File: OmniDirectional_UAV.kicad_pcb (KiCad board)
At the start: 2 copper layers, 60 parts, among them J10 UART, J11 ST-Link, J9 Conn_01x02, Q1 IRLML6402, Q2 BSS138, SW1 SW_DPDT_x2, SW2 SKRPACE, U1 DRV8835, U10 LXDC55FAAA-203, U11 LT1963AES3-3.3, U12 LPS25HB, U13 STM32F446RE, U2 DRV8835, U3 DRV8835, U4 DRV8835, U5 DRV8835, U6 DRV8835, U7 DRV8835, U8 DRV8835, U9 MPU9250

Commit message: update pcb
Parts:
- added J1: motor, Connector_PinSocket_1.27mm:PinSocket_1x02_P1.27mm_Vertical, F.Cu at (164.5, 29.1)
- added J2: motor, Connector_PinSocket_1.27mm:PinSocket_1x02_P1.27mm_Vertical, F.Cu at (83.5, 58.1)
- added J3: motor, Connector_PinSocket_1.27mm:PinSocket_1x02_P1.27mm_Vertical, F.Cu at (148.8, 58.0)
- added J4: motor, Connector_PinSocket_1.27mm:PinSocket_1x02_P1.27mm_Vertical, F.Cu at (150.2, 29.1)
- added J5: motor, Connector_PinSocket_1.27mm:PinSocket_1x02_P1.27mm_Vertical, F.Cu at (70.4, 30.1)
- added J6: motor, Connector_PinSocket_1.27mm:PinSocket_1x02_P1.27mm_Vertical, F.Cu at (85.2, 30.1)
- added J7: motor, Connector_PinSocket_1.27mm:PinSocket_1x02_P1.27mm_Vertical, F.Cu at (69.0, 58.2)
- added J8: motor, Connector_PinSocket_1.27mm:PinSocket_1x02_P1.27mm_Vertical, F.Cu at (163.3, 57.8)
- added SW3: SKRPACE, Button_Switch_SMD:SW_Push_1P1T_NO_Vertical_Wuerth_434133025816, F.Cu at (115.8, 57.9)
- J10: footprint Connector_PinHeader_2.54mm:PinHeader_1x04_P2.54mm_Horizontal -> Connector_PinHeader_2.54mm:PinHeader_1x04_P2.54mm_Vertical
- J11: footprint Connector_JST:JST_SH_BM04B-SRSS-TB_1x04-1MP_P1.00mm_Vertical -> Connector_JST:JST_SH_SM04B-SRSS-TB_1x04-1MP_P1.00mm_Horizontal
- moved U11 130.8 mm to (206.9, 38.7)
- moved J9 130.0 mm to (194.2, 58.1), turned to -90 degrees
- moved U7 126.4 mm to (69.6, 50.0)
- moved U10 119.1 mm to (186.4, 47.6), turned to 90 degrees
- moved C5 116.3 mm to (201.1, 36.8), turned to -90 degrees
- moved C6 112.6 mm to (201.2, 40.6), turned to 90 degrees
- moved U8 110.7 mm to (163.8, 49.0)
- moved U6 106.7 mm to (84.5, 38.7), turned to 180 degrees
- moved R3 105.6 mm to (195.6, 38.6)
- moved Q1 103.7 mm to (203.7, 48.8)
- moved R1 102.4 mm to (200.2, 48.8), turned to 90 degrees
- moved R5 101.5 mm to (207.4, 53.8), turned to -90 degrees
- moved C8 101.4 mm to (189.8, 38.5)
- moved R2 98.6 mm to (195.4, 36.1)
- moved D1 95.5 mm to (207.4, 58.0), turned to 90 degrees
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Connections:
- R5 pad 1: +5V -> +3.3V
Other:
- board outline added: 156.7 x 35.6 mm

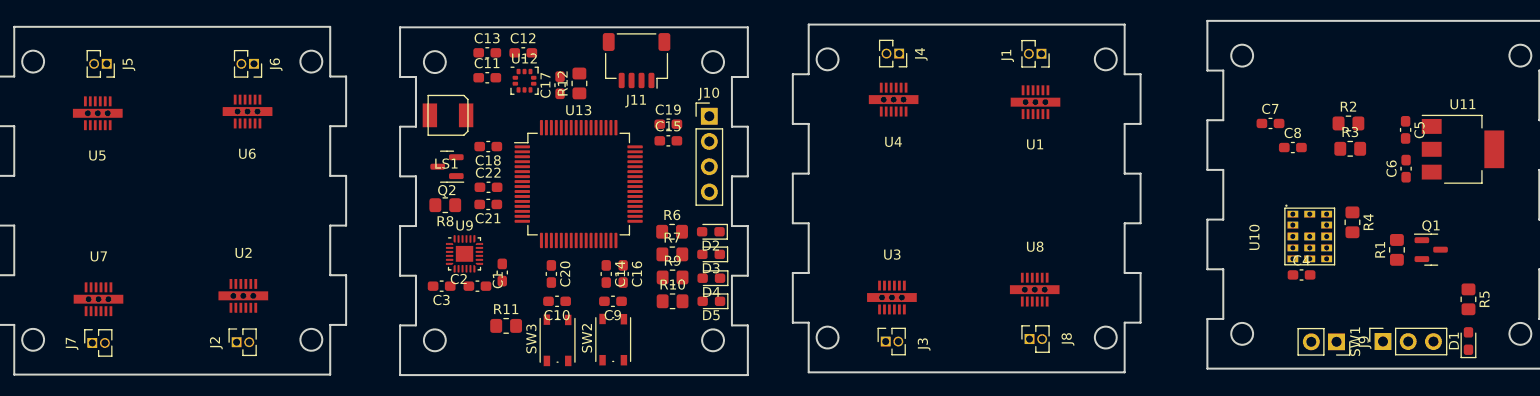
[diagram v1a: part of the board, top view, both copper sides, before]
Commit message: 部品配置完了
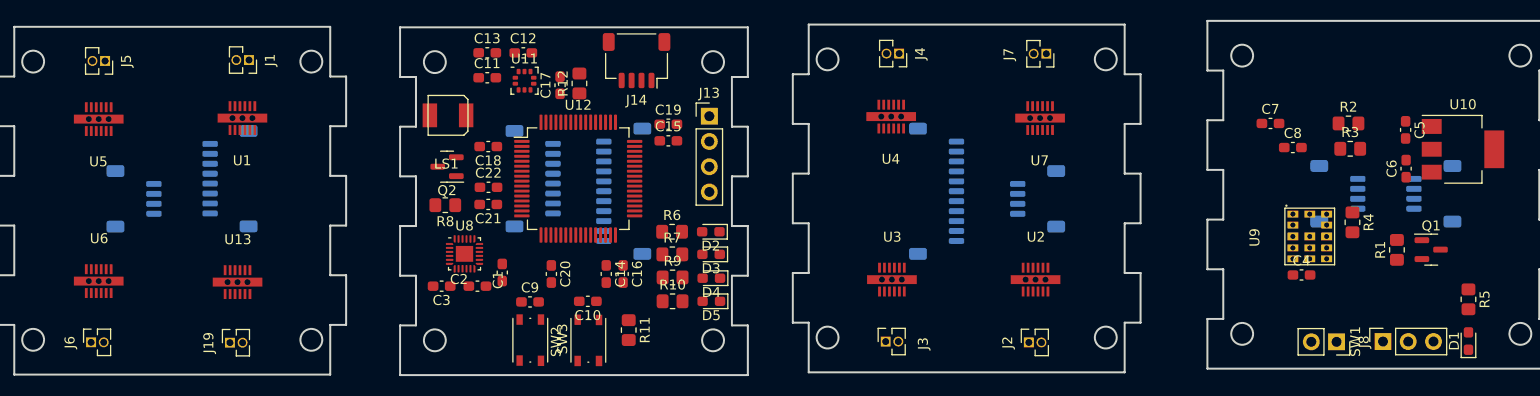
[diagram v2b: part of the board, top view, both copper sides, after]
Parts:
- removed the J7 at (69.0, 58.2)
- removed the U7 at (69.6, 50.0)
- added J10: conn, Connector_JST:JST_SH_SM04B-SRSS-TB_1x04-1MP_P1.00mm_Horizontal, B.Cu at (204.0, 43.2)
- added J11: conn, Connector_JST:JST_SH_SM04B-SRSS-TB_1x04-1MP_P1.00mm_Horizontal, B.Cu at (164.1, 43.7)
- added J12: conn, Connector_JST:JST_SH_SM04B-SRSS-TB_1x04-1MP_P1.00mm_Horizontal, B.Cu at (73.2, 43.7)
- added J15: Conn_01x08_Female, Connector_JST:JST_SH_SM08B-SRSS-TB_1x08-1MP_P1.00mm_Horizontal, B.Cu at (113.3, 41.7)
- added J16: Conn_01x11_Female, Connector_JST:JST_SH_SM11B-SRSS-TB_1x11-1MP_P1.00mm_Horizontal, B.Cu at (122.4, 42.9)
- added J17: Conn_01x08_Female, Connector_JST:JST_SH_SM08B-SRSS-TB_1x08-1MP_P1.00mm_Horizontal, B.Cu at (82.8, 41.7)
- added J18: Conn_01x11_Female, Connector_JST:JST_SH_SM11B-SRSS-TB_1x11-1MP_P1.00mm_Horizontal, B.Cu at (153.9, 42.9)
- added J19: motor, Connector_PinSocket_1.27mm:PinSocket_1x02_P1.27mm_Vertical, F.Cu at (82.8, 58.2)
- added J9: conn, Connector_JST:JST_SH_SM04B-SRSS-TB_1x04-1MP_P1.00mm_Horizontal, B.Cu at (194.3, 43.2)
- added U12: STM32F446RE, Package_QFP:LQFP-64_10x10mm_P0.5mm, F.Cu at (117.9, 41.7)
- U13: value STM32F446RE -> DRV8835; footprint Package_QFP:LQFP-64_10x10mm_P0.5mm -> omni:DRV8835
- moved U1 79.8 mm to (84.0, 39.3)
- moved J1 79.8 mm to (84.7, 29.7)
- moved U2 79.7 mm to (163.9, 48.0)
- moved J2 79.7 mm to (163.2, 58.1)
- moved U13 34.8 mm to (83.6, 48.3)
- moved J6 32.5 mm to (68.8, 58.1), turned to 90 degrees
- moved J7 28.8 mm to (165.0, 29.1), turned to -90 degrees
- moved U6 17.7 mm to (69.6, 48.2), turned to 0 degrees
- moved R11 12.3 mm to (122.9, 56.9), turned to -90 degrees
- moved U7 9.71 mm to (164.3, 39.3), turned to 180 degrees
- moved C9 8.35 mm to (113.0, 54.1), turned to 0 degrees
- moved SW2 8.35 mm to (113.0, 57.9), turned to -90 degrees
- moved C10 3.10 mm to (118.8, 54.0)
- moved SW3 3.10 mm to (118.9, 57.9)
- moved U3 1.80 mm to (149.5, 48.0)
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- renumbered J10 to J13, J11 to J14, J8 to J7, J9 to J8, U11 to U10, U12 to U11, U8 to U7, U9 to U8, U10 to U9
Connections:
- C21 pad 1: +3.3VADC -> +3.3V
- C22 pad 1: +3.3VADC -> +3.3V
- C4 pad 2: GND -> GND_
- C5 pad 2: GND -> GND_
- C6 pad 1: +3.3V -> +3.3V_
- C6 pad 2: GND -> GND_
- C7 pad 2: GND -> GND_
- C8 pad 2: GND -> GND_
- D1 pad 1: GND -> GND_
- J8 pad 2: GND -> GND_
- R2 pad 2: /controller/ADC_BAT -> _ADC_BAT
- R3 pad 1: /controller/ADC_BAT -> _ADC_BAT
- R3 pad 2: GND -> GND_
- R4 pad 2: GND -> GND_
- R5 pad 1: +3.3V -> +3.3V_
- SW1 pad 1: GND -> unconnected-(SW1-Pad1)
- U1 pad 1: +BATT -> /motor2/+BATT_2
- U1 pad 10: /controller/MOTOR2_IN1 -> /controller/MOTOR5_IN1
- U1 pad 11: GND -> /motor2/GND_2
- U1 pad 12: +3.3V -> /motor2/+3.3V_2
- U1 pad 13: GND -> /motor2/GND_2
- U1 pad 6: GND -> /motor2/GND_2
- U1 pad 7: /controller/MOTOR2_IN2 -> /controller/MOTOR5_IN2
- U1 pad 8: /controller/MOTOR2_IN1 -> /controller/MOTOR5_IN1
- U1 pad 9: /controller/MOTOR2_IN2 -> /controller/MOTOR5_IN2
- U10 pad 2: GND -> GND_
- U10 pad 3: +3.3V -> +3.3V_
- U10 pad 4: GND -> GND_
- U13 pad 1: +3.3V -> /motor2/+BATT_2
- U13 pad 10: /controller/SPI3_CS -> /controller/MOTOR2_IN1
- U13 pad 11: unconnected-(U13-Pad11) -> /motor2/GND_2
- U13 pad 12: GND -> /motor2/+3.3V_2
- U13 pad 13: +3.3VADC -> /motor2/GND_2
- U13 pad 2: unconnected-(U13-Pad2) -> Net-(J19-Pad1)
- U13 pad 3: unconnected-(U13-Pad3) -> Net-(J19-Pad2)
- U13 pad 4: unconnected-(U13-Pad4) -> Net-(J19-Pad1)
- U13 pad 5: unconnected-(U13-Pad5) -> Net-(J19-Pad2)
- U13 pad 6: unconnected-(U13-Pad6) -> /motor2/GND_2
- U13 pad 7: /controller/NRST -> /controller/MOTOR2_IN2
- U13 pad 8: unconnected-(U13-Pad8) -> /controller/MOTOR2_IN1
- U13 pad 9: /controller/SPI3_MOSI -> /controller/MOTOR2_IN2
- U2 pad 1: +BATT -> /motor1/+BATT_1
- U2 pad 11: GND -> /controller/GND_
- U2 pad 12: +3.3V -> /controller/+3.3V_
- U2 pad 13: GND -> /controller/GND_
- U2 pad 6: GND -> /controller/GND_
- U3 pad 1: +BATT -> /motor1/+BATT_1
- U3 pad 11: GND -> /controller/GND_
- U3 pad 12: +3.3V -> /controller/+3.3V_
- U3 pad 13: GND -> /controller/GND_
- U3 pad 6: GND -> /controller/GND_
- U4 pad 1: +BATT -> /motor1/+BATT_1
- U4 pad 11: GND -> /controller/GND_
- U4 pad 12: +3.3V -> /controller/+3.3V_
- U4 pad 13: GND -> /controller/GND_
- U4 pad 6: GND -> /controller/GND_
- U5 pad 1: +BATT -> /motor2/+BATT_2
- U5 pad 10: /controller/MOTOR5_IN1 -> /controller/MOTOR6_IN1
- U5 pad 11: GND -> /motor2/GND_2
- U5 pad 12: +3.3V -> /motor2/+3.3V_2
- U5 pad 13: GND -> /motor2/GND_2
- U5 pad 6: GND -> /motor2/GND_2
- U5 pad 7: /controller/MOTOR5_IN2 -> /controller/MOTOR6_IN2
- U5 pad 8: /controller/MOTOR5_IN1 -> /controller/MOTOR6_IN1
- U5 pad 9: /controller/MOTOR5_IN2 -> /controller/MOTOR6_IN2
- U6 pad 1: +BATT -> /motor2/+BATT_2
- U6 pad 10: /controller/MOTOR6_IN1 -> /controller/MOTOR7_IN1
- U6 pad 11: GND -> /motor2/GND_2
- U6 pad 12: +3.3V -> /motor2/+3.3V_2
- U6 pad 13: GND -> /motor2/GND_2
- U6 pad 6: GND -> /motor2/GND_2
- U6 pad 7: /controller/MOTOR6_IN2 -> /controller/MOTOR7_IN2
- U6 pad 8: /controller/MOTOR6_IN1 -> /controller/MOTOR7_IN1
- U6 pad 9: /controller/MOTOR6_IN2 -> /controller/MOTOR7_IN2
- U7 pad 1: +BATT -> /motor1/+BATT_1
- U7 pad 11: GND -> /controller/GND_
- U7 pad 12: +3.3V -> /controller/+3.3V_
- U7 pad 13: GND -> /controller/GND_
- U7 pad 6: GND -> /controller/GND_
- U9 pad 10: GND -> GND_
- U9 pad 12: GND -> GND_
- U9 pad 13: GND -> GND_
- U9 pad 14: GND -> GND_
- U9 pad 6: GND -> GND_
